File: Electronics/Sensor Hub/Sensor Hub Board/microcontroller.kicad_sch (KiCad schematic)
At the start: 57 parts, among them IC301 STM32H723ZGT6, IC302 TJA1057GT/3, IC303 TJA1057GT/3, IC304 TJA1057GT/3, J301 TC2030, J302 MEM2075-00-140-01-A, J303 TYPE-C-31-M-12, J304 Screw_Terminal_01x02, J305 Screw_Terminal_01x02, J306 Screw_Terminal_01x02, SW301 SW_DIP_x02, U301 USBLC6-4SC6-ES, U302 USBLC6-4SC6-ES, X301 25MHz_Clock, X302 25MHz_Clock, X303 32.768kHz_Clock

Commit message: PCB Schematics finished
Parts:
- removed C301: 100n, Capacitor_SMD:C_0402_1005Metric, symbol Device:C_Small
- removed C325: 10u, Capacitor_SMD:C_0402_1005Metric, symbol Device:C_Small
- removed FL301: EMIF06-MSD02N16, EMIF06MSD02N16, symbol EMIF06-MSD02N16:EMIF06-MSD02N16
- removed IC303, IC304: TJA1057GT/3, SOIC127P600X175-8N, symbol TJA1057T:TJA1057GT/3
- removed J302: MEM2075-00-140-01-A, MEM20750014001A, symbol MEM2075-00-140-01-A:MEM2075-00-140-01-A
- removed J305, J306: Screw_Terminal_01x02, TerminalBlock:TerminalBlock_bornier-2_P5.08mm, symbol Connector:Screw_Terminal_01x02
- removed R6: 5k1, Resistor_SMD:R_0402_1005Metric, symbol Device:R_Small
- removed R6 (x2): 120R, Resistor_SMD:R_0402_1005Metric, symbol Device:R_Small
- removed X301: 25MHz_Clock, Oscillator:Oscillator_SMD_Abracon_ASE-4Pin_3.2x2.5mm_HandSoldering, symbol MSL_Symbols:25MHz_Clock
- added FB1: 120R@100MHz, Resistor_SMD:R_0402_1005Metric, symbol Device:FerriteBead_Small
- added R6: 5k1, Resistor_SMD:R_0402_1005Metric, symbol Device:R_Small
- added R6 (x4): 2k2, Resistor_SMD:R_0402_1005Metric, symbol Device:R_Small
- renumbered C303 to C301, C305 to C304, C306 to C305, C307 to C306, C308 to C307, C309 to C308, C310 to C309, C311 to C310, C312 to C311, C313 to C312, C314 to C313, C315 to C314, C316 to C315, C317 to C316, C318 to C317, C319 to C318, C323 to C319, C324 to C323, IC302 to IC301, IC301 to IC302, J304 to J302, X302 to X301, X303 to X302
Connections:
- net +3V3: now also C301.1, FB1.2, R6.1, R6.1, R6.1, R6.1; no longer C301.2, C307.1, C309.1, IC302.33 (VDDA)
- net CC1: now also R6.1
- net GND: now also C301.2, R6.2; no longer C301.1
- net OSC32K: now also X302.3 (OUT)
- net VREF+: now also C307.1, C309.1, IC302.33 (VDDA), FB1.1
- net SDA2_MCU: now reaches IC302.10 (PF0)
- net SDA2_MCU: now also R6.2
- net SCL2_MCU: now reaches IC302.11 (PF1)
- net SCL2_MCU: now also R6.2
- net SDA1_MCU: now reaches IC302.137 (PB7)
- net SDA1_MCU: now also R6.2
- net IMU_CS: now reaches IC302.40 (PA4)
- net IMU_SCK: now reaches IC302.41 (PA5)
- net IMU_MISO: now reaches IC302.42 (PA6)
- net MAG_MISO: now reaches IC302.75 (PB14)
- net MAG_MOSI: now reaches IC302.76 (PB15)
- net CANH1 renamed CANH
- net CANL1 renamed CANL
- net CAN_RX1 renamed CAN_RX
- net CAN_RX2: no longer names the net of IC302.135 (PB5)
- net CAN_RX3: no longer names the net of IC302.18 (PF6)
- net CAN_TX1 renamed CAN_TX
- net CAN_TX2 renamed SCL1_MCU
- net SCL1_MCU: now also R6.2
- net CAN_TX3: no longer names the net of IC302.19 (PF7)
- net ETH_CRS_DV renamed IMU_MOSI
- net ETH_MDC: no longer names the net of IC302.27 (PC1)
- net ETH_MDIO: no longer names the net of IC302.36 (PA2)
- net ETH_REF_CLK: no longer names the net of IC302.35 (PA1)
- net ETH_REF_CLK: no longer X302.3 (OUT)
- net ETH_RXD0: no longer names the net of IC302.44 (PC4)
- net ETH_RXD1: no longer names the net of IC302.45 (PC5)
- net ETH_TXD0 renamed MAG_CS
- net ETH_TXD1 renamed MAG_SCK
- net ETH_TX_EN: no longer names the net of IC302.70 (PB11)
- net SDMMC1_CD: no longer names the net of IC302.100 (PA8)
- net SDMMC1_CLK: no longer names the net of IC302.113 (PC12)
- net SDMMC1_CMD: no longer names the net of IC302.116 (PD2)
- net SDMMC1_DAT0: no longer names the net of IC302.98 (PC8)
- net SDMMC1_DAT1: no longer names the net of IC302.99 (PC9)
- net SDMMC1_DAT2: no longer names the net of IC302.111 (PC10)
- net SDMMC1_DAT3: no longer names the net of IC302.112 (PC11)
- net SILENT1 renamed SILENT
- no-connect marks 11 -> 9
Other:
- note added: "CAN Transceiver"
- note added: "I2C Pullup Resistors"
- note added: "User Buttons"
- note removed: "CAN Transceivers"
- note removed: "Micro SD Card Slot"
- note removed: "User Button"
- moved on the sheet: C301, C304, C305, C306, C307, C308, C309, C310, C311, C312, C313, C314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

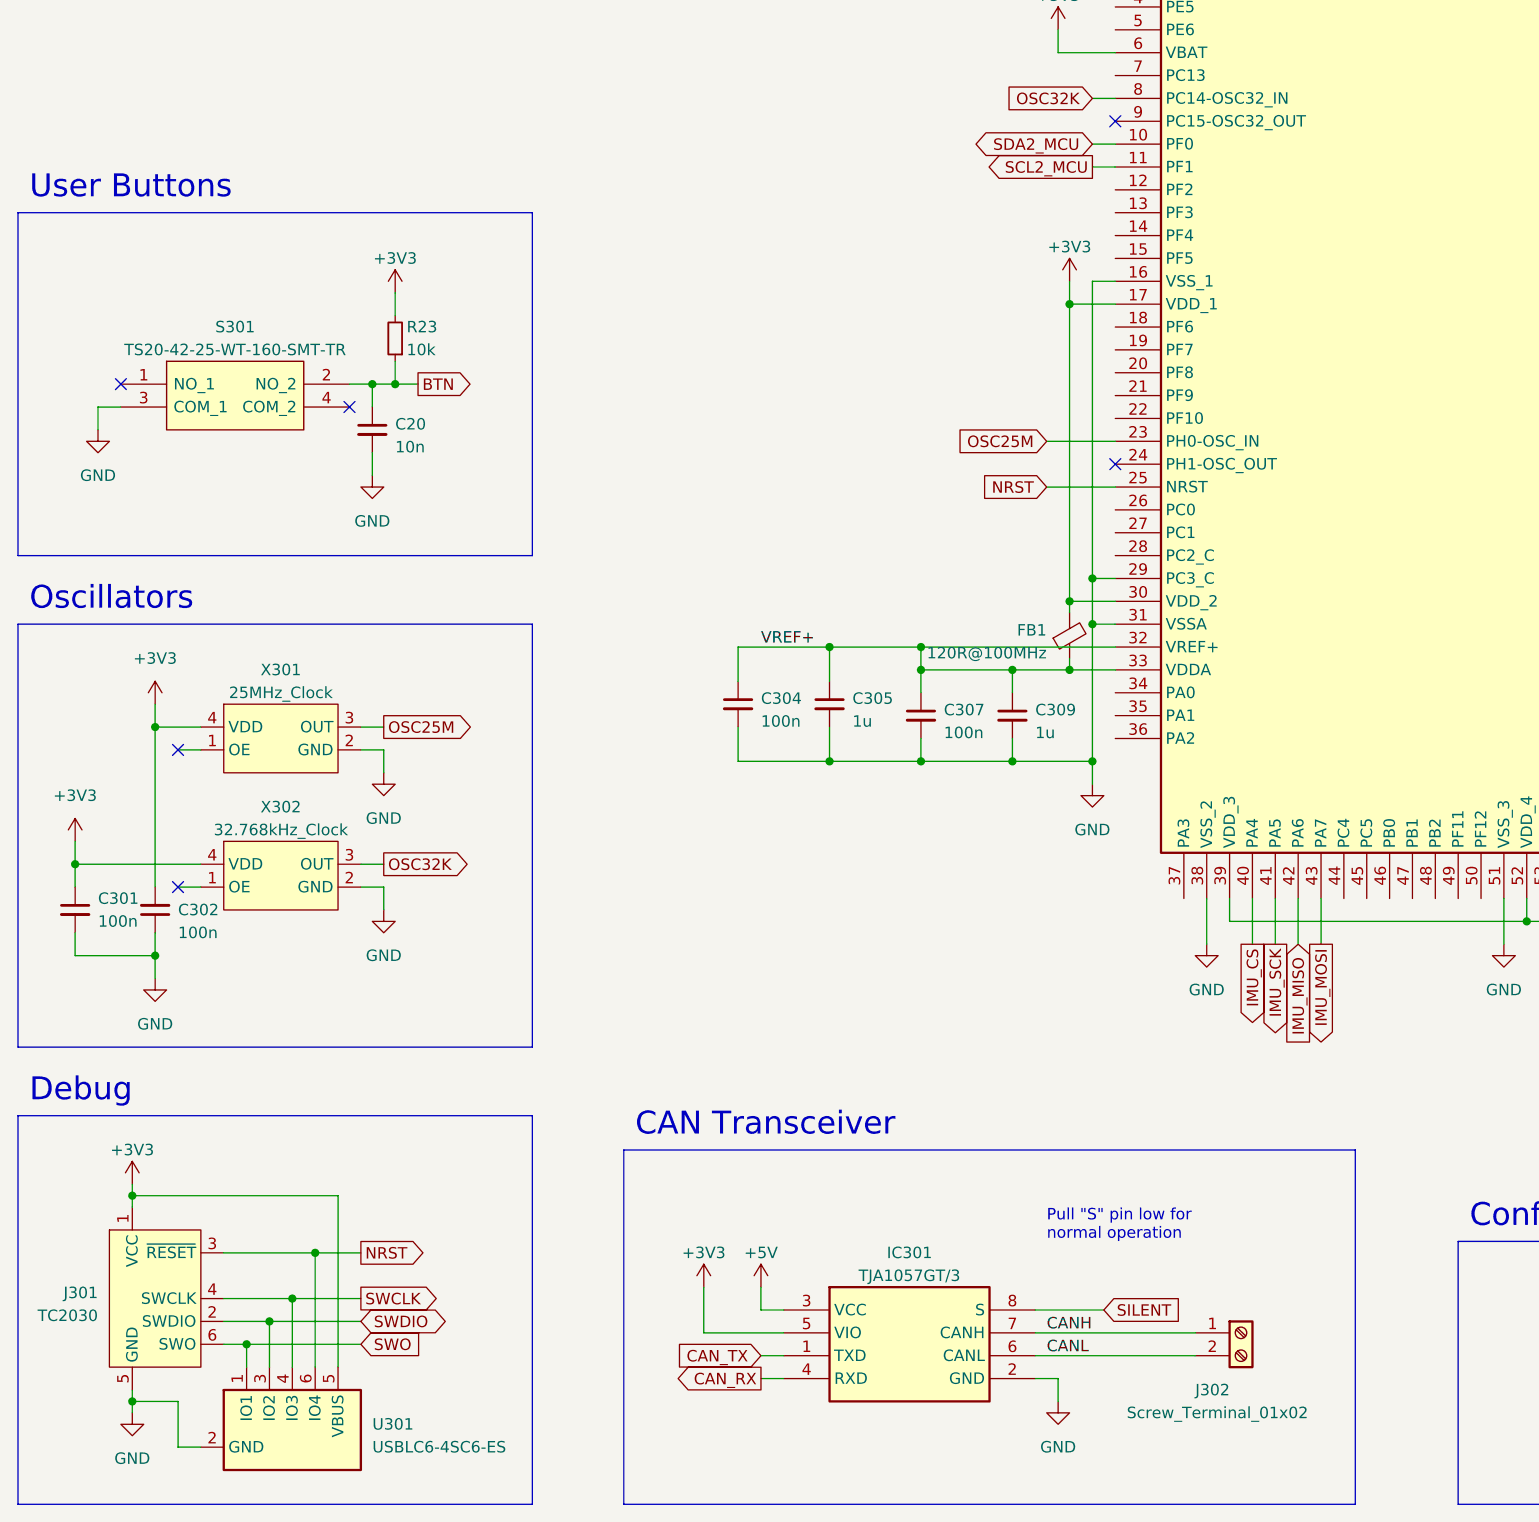
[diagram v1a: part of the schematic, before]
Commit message: Schematic updates
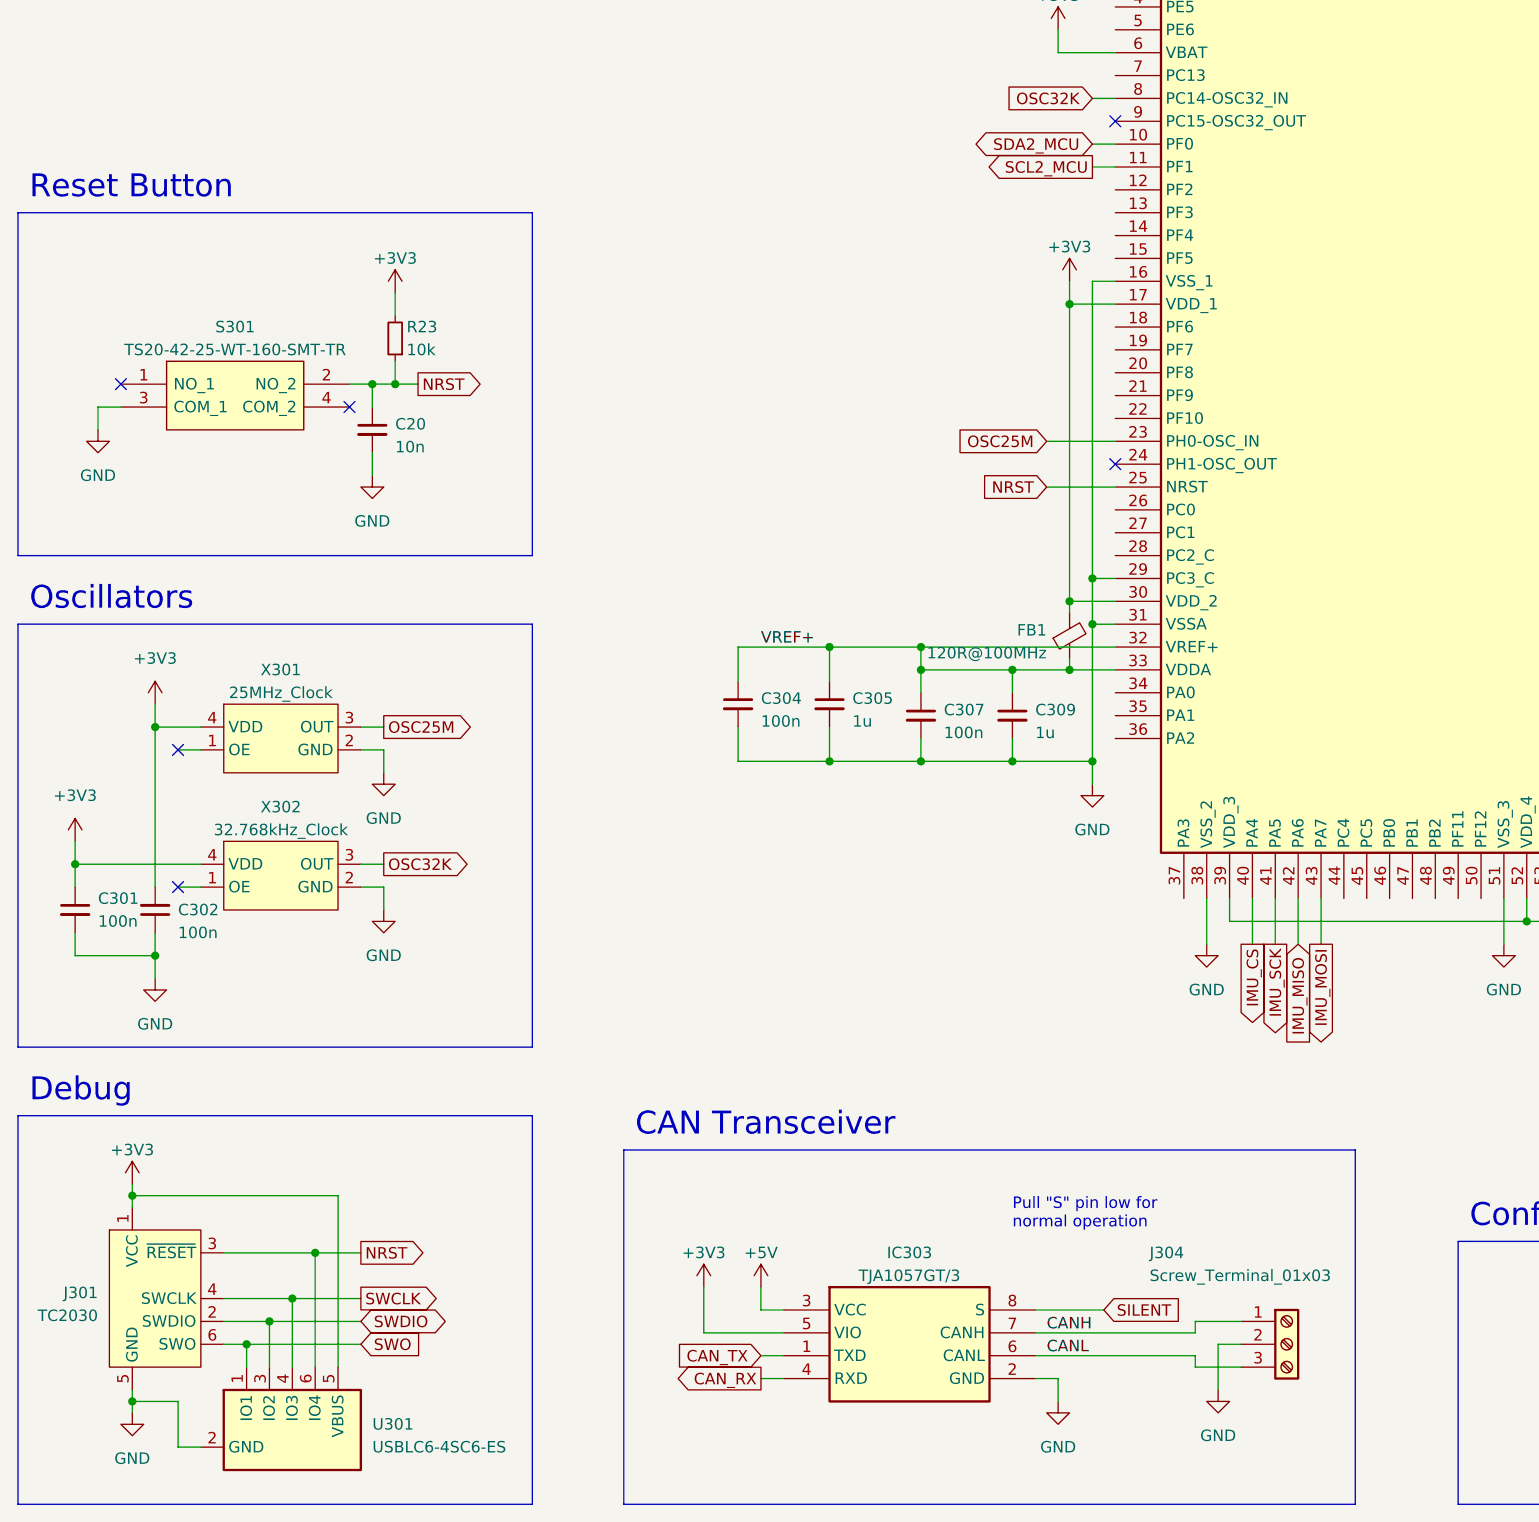
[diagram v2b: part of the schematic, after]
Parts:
- removed IC301: TJA1057GT/3, SOIC127P600X175-8N, symbol TJA1057T:TJA1057GT/3
- removed J302: Screw_Terminal_01x02, TerminalBlock:TerminalBlock_bornier-2_P5.08mm, symbol Connector:Screw_Terminal_01x02
- added IC303: TJA1057GT/3, SOIC127P600X175-8N, symbol TJA1057T:TJA1057GT/3
- added J304: Screw_Terminal_01x03, TerminalBlock:TerminalBlock_bornier-3_P5.08mm, symbol Connector:Screw_Terminal_01x03
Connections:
- net +3V3: now also IC303.5 (VIO)
- net +5V: now also IC303.3 (VCC)
- net BTN: no longer C20.1, R23.1, S301.2 (NO_2)
- net CANH: now also IC303.7 (CANH), J304.1 (Pin_1)
- net CANL: now also IC303.6 (CANL), J304.3 (Pin_3)
- net CAN_RX: now also IC303.4 (RXD)
- net CAN_TX: now also IC303.1 (TXD)
- net GND: now also IC303.2 (GND), J304.2 (Pin_2)
- net NRST: now also C20.1, R23.1, S301.2 (NO_2)
- net SILENT: now also IC303.8 (S)
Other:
- note added: "Reset Button"
- note removed: "User Buttons"

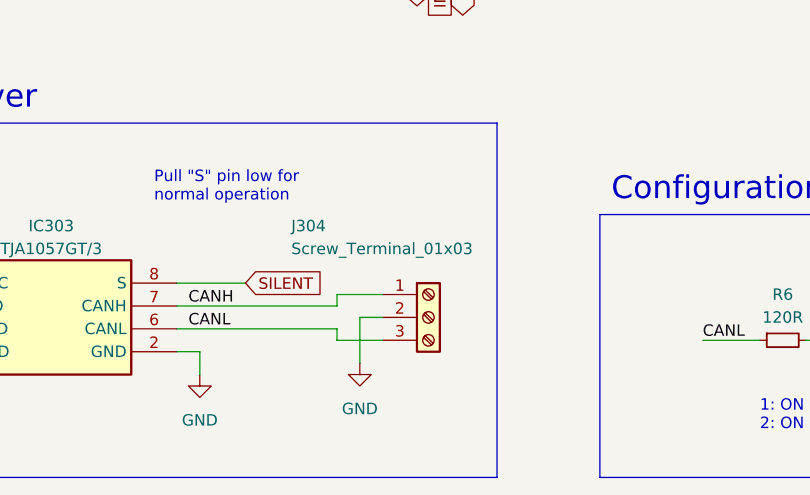
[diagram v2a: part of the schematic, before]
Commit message: PCB layout progress, spice simulations for power board
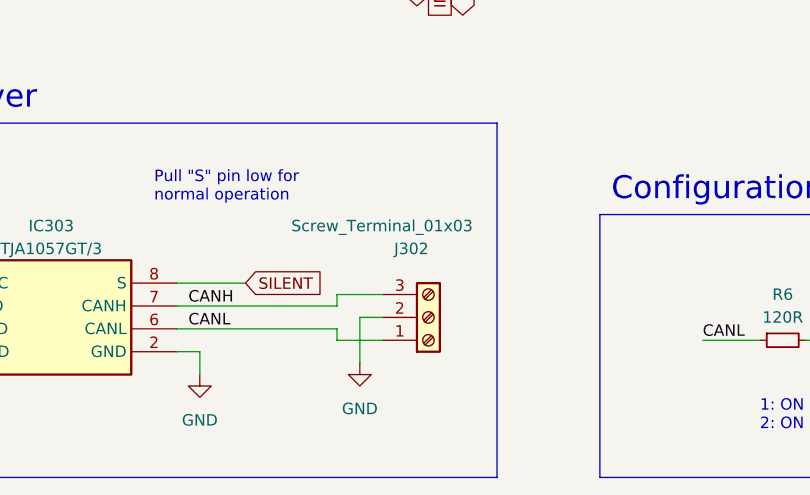
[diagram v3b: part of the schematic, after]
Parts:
- removed J304: Screw_Terminal_01x03, TerminalBlock:TerminalBlock_bornier-3_P5.08mm, symbol Connector:Screw_Terminal_01x03
- added J302: Screw_Terminal_01x03, TerminalBlock:TerminalBlock_bornier-3_P5.08mm, symbol Connector:Screw_Terminal_01x03
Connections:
- net CANH: now also J302.3 (Pin_3)
- net CANL: now also J302.1 (Pin_1)
- net GND: now also J302.2 (Pin_2)
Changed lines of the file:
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@@
-    )
-  )
-  (symbol (lib_id "Connector:Screw_Terminal_01x03") (at 160.02 261.62 0) (unit 1)
-    (in_bom yes) (on_board yes) (dnp no)
-    (property "Reference" "J304" (at 144.78 251.46 0)
-      (effects (font (size 1.27 1.27)) (justify left))
-    )
-    (property "Value" "Screw_Terminal_01x03" (at 144.78 254 0)
-      (effects (font (size 1.27 1.27)) (justify left))
-    )
-    (property "Footprint" "TerminalBlock:TerminalBlock_bornier-3_P5.08mm" (at 160.02 261.62 0)
-      (effects (font (size 1.27 1.27)) hide)
-    )
-    (property "Datasheet" "~" (at 160.02 261.62 0)
-      (effects (font (size 1.27 1.27)) hide)
-    )
-    (pin "1")
-    (pin "2")
-    (pin "3")
-    (instances
-      (project "Sensor Hub Board"
-        (path "/5318664d-e328-4e84-a383-7318275dc447/86a04d6c-5487-4291-b767-6da69e96f7da"
-          (reference "J304") (unit 1)
-        )
-      )
-      (project "Power Board"
-        (path "/d8843e0a-fd8a-4193-ba57-f0164156e030/fab43204-4de8-48e9-a4c9-80bcd4a9c27a"
-          (reference "J303") (unit 1)
-        )
-      )
     )
   )
@@
         )
       )
+    )
+  )
+  (symbol (lib_id "Connector:Screw_Terminal_01x03") (at 160.02 261.62 0) (mirror x) (unit 1)
+    (in_bom yes) (on_board yes) (dnp no)
+    (property "Reference" "J302" (at 156.21 254 0)
+      (effects (font (size 1.27 1.27)) (justify left))
+    )
+    (property "Value" "Screw_Terminal_01x03" (at 144.78 251.46 0)
+      (effects (font (size 1.27 1.27)) (justify left))
+    )
+    (property "Footprint" "TerminalBlock:TerminalBlock_bornier-3_P5.08mm" (at 160.02 261.62 0)
+      (effects (font (size 1.27 1.27)) hide)
+    )
+    (property "Datasheet" "~" (at 160.02 261.62 0)
+      (effects (font (size 1.27 1.27)) hide)
+    )
+    (pin "1")
+    (pin "2")
+    (pin "3")
+    (instances
+      (project "Sensor Hub Board"
+        (path "/5318664d-e328-4e84-a383-7318275dc447/86a04d6c-5487-4291-b767-6da69e96f7da"
+          (reference "J302") (unit 1)
+        )
+      )
+      (project "Power Board"
+        (path "/d8843e0a-fd8a-4193-ba57-f0164156e030/fab43204-4de8-48e9-a4c9-80bcd4a9c27a"
+          (reference "J303") (unit 1)
+        )
+      )
